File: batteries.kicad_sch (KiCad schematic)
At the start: 14 parts, among them J3 67996-110HLF

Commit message: general fixes #3 #4
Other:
- moved on the sheet: RTD1, RTD2, RTD3
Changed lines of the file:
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@@
     (effects (font (face "KiCad Font") (size 4 4)) (justify left bottom))
   )
-  (text "RTS SENSORS\n" (at 116.84 43.18 0)
+  (text "RTS SENSORS\n" (at 36.83 33.02 0)
     (effects (font (face "KiCad Font") (size 4 4)) (justify left bottom))
   )
@@
     )
   )
-  (global_label "RTD_common" (shape input) (at 132.08 76.2 180) (fields_autoplaced)
-    (effects (font (size 1.27 1.27)) (justify right))
-    (property "Intersheetrefs" "${INTERSHEET_REFS}" (at 116.6974 76.2 0)
+  (global_label "RTD_common" (shape input) (at 52.07 66.04 180) (fields_autoplaced)
+    (effects (font (size 1.27 1.27)) (justify right))
+    (property "Intersheetrefs" "${INTERSHEET_REFS}" (at 36.6874 66.04 0)
       (effects (font (size 1.27 1.27)) (justify right) hide)
     )
@@
     )
   )
-  (global_label "RTD3" (shape input) (at 142.24 76.2 0) (fields_autoplaced)
-    (effects (font (size 1.27 1.27)) (justify left))
-    (property "Intersheetrefs" "${INTERSHEET_REFS}" (at 149.9423 76.2 0)
+  (global_label "RTD3" (shape input) (at 62.23 66.04 0) (fields_autoplaced)
+    (effects (font (size 1.27 1.27)) (justify left))
+    (property "Intersheetrefs" "${INTERSHEET_REFS}" (at 69.9323 66.04 0)
       (effects (font (size 1.27 1.27)) (justify left) hide)
     )
@@
     )
   )
-  (global_label "RTD6" (shape input) (at 142.24 88.9 0) (fields_autoplaced)
-    (effects (font (size 1.27 1.27)) (justify left))
-    (property "Intersheetrefs" "${INTERSHEET_REFS}" (at 149.9423 88.9 0)
-      (effects (font (size 1.27 1.27)) (justify left) hide)
-    )
-  )
-  (global_label "RTD_common" (shape input) (at 132.08 88.9 180) (fields_autoplaced)
-    (effects (font (size 1.27 1.27)) (justify right))
-    (property "Intersheetrefs" "${INTERSHEET_REFS}" (at 116.6974 88.9 0)
+  (global_label "RTD6" (shape input) (at 62.23 78.74 0) (fields_autoplaced)
+    (effects (font (size 1.27 1.27)) (justify left))
+    (property "Intersheetrefs" "${INTERSHEET_REFS}" (at 69.9323 78.74 0)
+      (effects (font (size 1.27 1.27)) (justify left) hide)
+    )
+  )
+  (global_label "RTD_common" (shape input) (at 52.07 78.74 180) (fields_autoplaced)
+    (effects (font (size 1.27 1.27)) (justify right))
+    (property "Intersheetrefs" "${INTERSHEET_REFS}" (at 36.6874 78.74 0)
       (effects (font (size 1.27 1.27)) (justify right) hide)
     )
@@
     )
   )
-  (global_label "RTD2" (shape input) (at 142.24 63.5 0) (fields_autoplaced)
-    (effects (font (size 1.27 1.27)) (justify left))
-    (property "Intersheetrefs" "${INTERSHEET_REFS}" (at 149.9423 63.5 0)
+  (global_label "RTD2" (shape input) (at 62.23 53.34 0) (fields_autoplaced)
+    (effects (font (size 1.27 1.27)) (justify left))
+    (property "Intersheetrefs" "${INTERSHEET_REFS}" (at 69.9323 53.34 0)
       (effects (font (size 1.27 1.27)) (justify left) hide)
     )
@@
     )
   )
-  (global_label "RTD_common" (shape input) (at 132.08 63.5 180) (fields_autoplaced)
-    (effects (font (size 1.27 1.27)) (justify right))
-    (property "Intersheetrefs" "${INTERSHEET_REFS}" (at 116.6974 63.5 0)
+  (global_label "RTD_common" (shape input) (at 52.07 53.34 180) (fields_autoplaced)
+    (effects (font (size 1.27 1.27)) (justify right))
+    (property "Intersheetrefs" "${INTERSHEET_REFS}" (at 36.6874 53.34 0)
       (effects (font (size 1.27 1.27)) (justify right) hide)
     )
@@
     )
   )
-  (symbol (lib_id "Device:Thermistor") (at 137.16 88.9 90) (unit 1)
-    (in_bom yes) (on_board yes) (dnp no) (fields_autoplaced)
-    (property "Reference" "RTD1" (at 137.16 82.55 90)
-      (effects (font (size 1.27 1.27)))
-    )
-    (property "Value" "Thermistor" (at 137.16 85.09 90)
-      (effects (font (size 1.27 1.27)))
-    )
-    (property "Footprint" "" (at 137.16 88.9 0)
-      (effects (font (size 1.27 1.27)) hide)
-    )
-    (property "Datasheet" "~" (at 137.16 88.9 0)
+  (symbol (lib_id "Device:Thermistor") (at 57.15 78.74 90) (unit 1)
+    (in_bom yes) (on_board yes) (dnp no) (fields_autoplaced)
+    (property "Reference" "RTD1" (at 57.15 72.39 90)
+      (effects (font (size 1.27 1.27)))
+    )
+    (property "Value" "Thermistor" (at 57.15 74.93 90)
+      (effects (font (size 1.27 1.27)))
+    )
+    (property "Footprint" "" (at 57.15 78.74 0)
+      (effects (font (size 1.27 1.27)) hide)
+    )
+    (property "Datasheet" "~" (at 57.15 78.74 0)
       (effects (font (size 1.27 1.27)) hide)
     )
@@
     )
   )
-  (symbol (lib_id "Device:Thermistor") (at 137.16 63.5 90) (unit 1)
-    (in_bom yes) (on_board yes) (dnp no) (fields_autoplaced)
-    (property "Reference" "RTD2" (at 137.16 57.15 90)
-      (effects (font (size 1.27 1.27)))
-    )
-    (property "Value" "Thermistor" (at 137.16 59.69 90)
-      (effects (font (size 1.27 1.27)))
-    )
-    (property "Footprint" "" (at 137.16 63.5 0)
-      (effects (font (size 1.27 1.27)) hide)
-    )
-    (property "Datasheet" "~" (at 137.16 63.5 0)
+  (symbol (lib_id "Device:Thermistor") (at 57.15 53.34 90) (unit 1)
+    (in_bom yes) (on_board yes) (dnp no) (fields_autoplaced)
+    (property "Reference" "RTD2" (at 57.15 46.99 90)
+      (effects (font (size 1.27 1.27)))
+    )
+    (property "Value" "Thermistor" (at 57.15 49.53 90)
+      (effects (font (size 1.27 1.27)))
+    )
+    (property "Footprint" "" (at 57.15 53.34 0)
+      (effects (font (size 1.27 1.27)) hide)
+    )
+    (property "Datasheet" "~" (at 57.15 53.34 0)
       (effects (font (size 1.27 1.27)) hide)
     )
@@
     )
   )
-  (symbol (lib_id "Device:Thermistor") (at 137.16 76.2 90) (unit 1)
-    (in_bom yes) (on_board yes) (dnp no) (fields_autoplaced)
-    (property "Reference" "RTD3" (at 137.16 69.85 90)
-      (effects (font (size 1.27 1.27)))
-    )
-    (property "Value" "Thermistor" (at 137.16 72.39 90)
-      (effects (font (size 1.27 1.27)))
-    )
-    (property "Footprint" "" (at 137.16 76.2 0)
-      (effects (font (size 1.27 1.27)) hide)
-    )
-    (property "Datasheet" "~" (at 137.16 76.2 0)
-      (effects (font (size 1.27 1.27)) hide)
-    )
+  (symbol (lib_id "Device:Thermistor") (at 57.15 66.04 90) (unit 1)
+    (in_bom yes) (on_board yes) (dnp no) (fields_autoplaced)
+    (property "Reference" "RTD3" (at 57.15 59.69 90)
+      (effects (font (size 1.27 1.27)))
+    )
+    (property "Value" "Thermistor" (at 57.15 62.23 90)
+      (effects (font (size 1.27 1.27)))
+    )
+    (property "Footprint" "" (at 57.15 66.04 0)
+      (effects (font (size 1.27 1.27)) hide)
+    )
+    (property "Datasheet" "~" (at 57.15 66.04 0)
+      (effects (font (size 1.27 1.27)) hide)
+    )

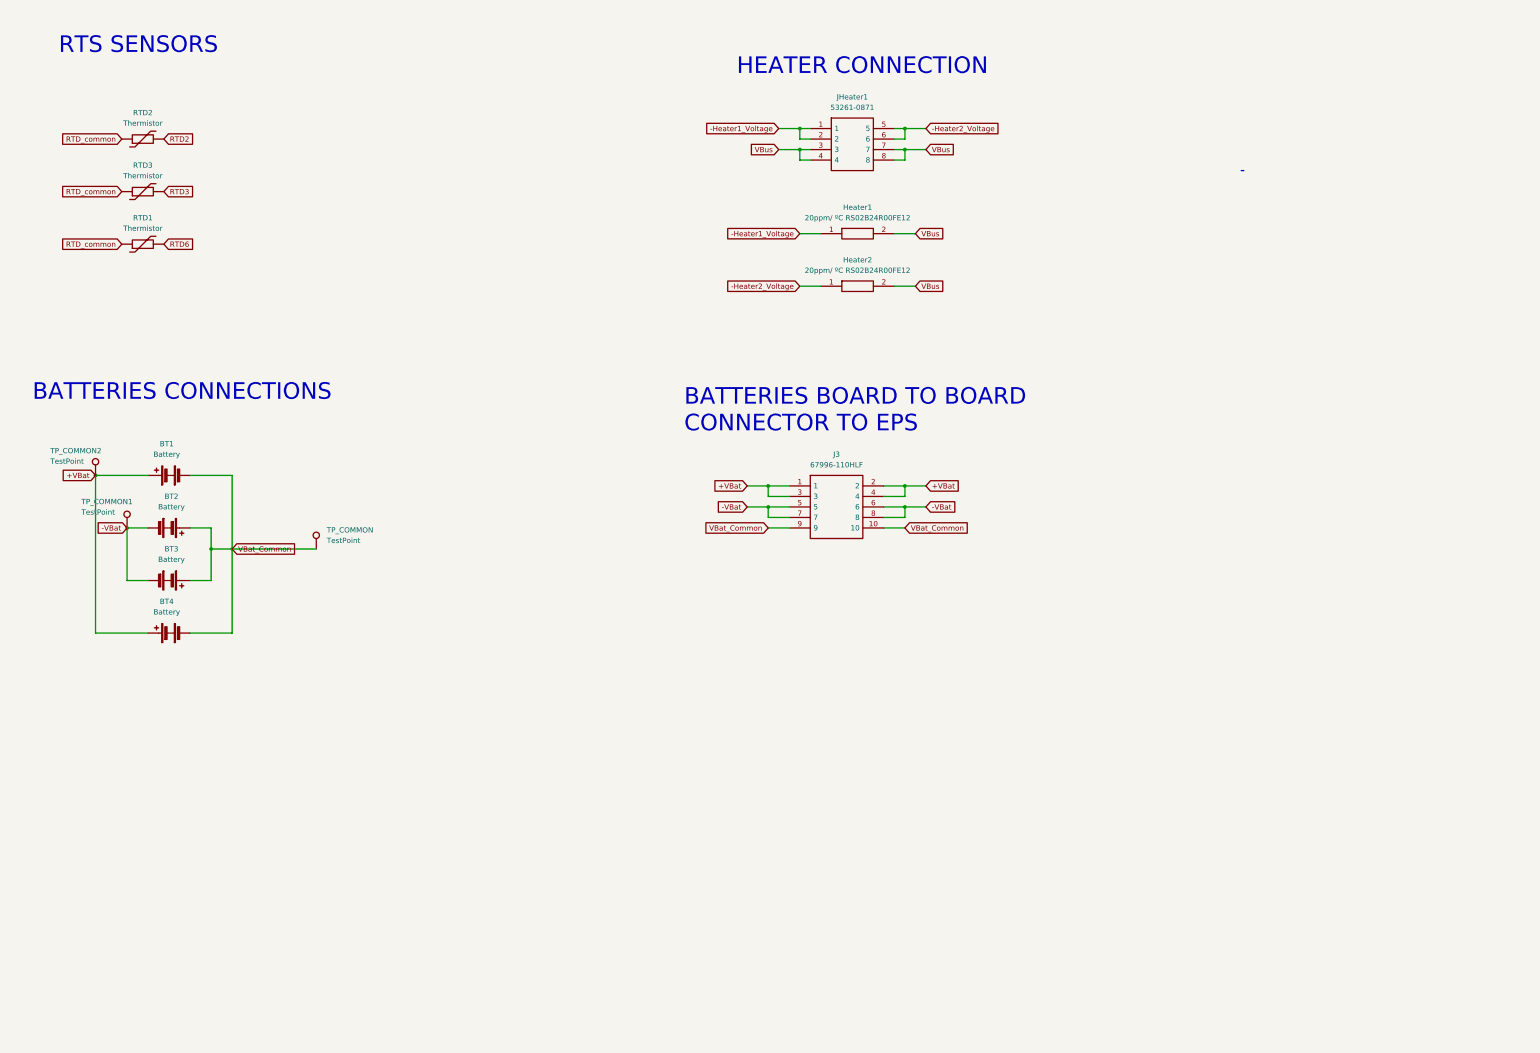
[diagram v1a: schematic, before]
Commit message: developing rtd and heater circuits
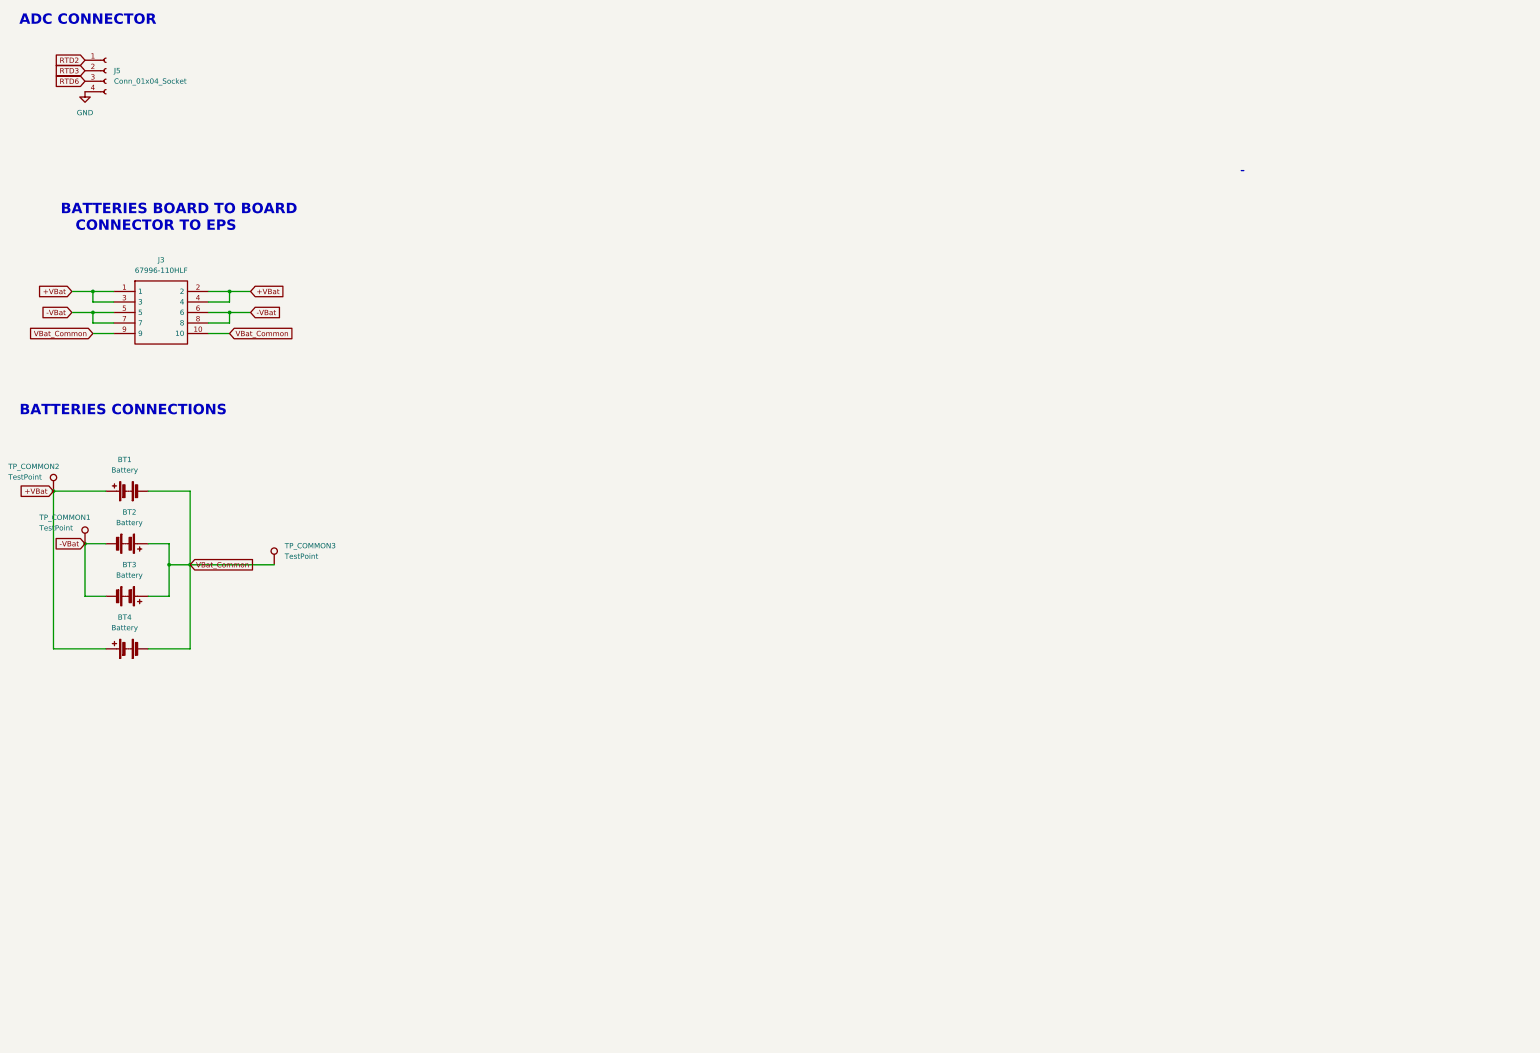
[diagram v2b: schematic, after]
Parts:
- removed Heater1, Heater2: 20ppm/ ºC RS02B24R00FE12, symbol RS02B24R00FE12:RS02B24R00FE12
- removed JHeater1: 53261-0871, symbol 53261-0871:53261-0871
- removed RTD1, RTD2, RTD3: Thermistor, symbol Device:Thermistor
- added J5: Conn_01x04_Socket, symbol Connector:Conn_01x04_Socket
- J3: footprint (none) -> lib:67996-110HLF
- renumbered TP_COMMON to TP_COMMON3
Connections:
- net RTD2: now also J5.1 (Pin_1)
- net RTD3: now also J5.2 (Pin_2)
- net RTD6: now also J5.3 (Pin_3)
- new net GND: J5.4 (Pin_4)
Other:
- note added: "ADC CONNECTOR"
- note removed: "HEATER CONNECTION"
- note removed: "RTS SENSORS"
- moved on the sheet: BT1, BT2, BT3, BT4, J3, TP_COMMON1, TP_COMMON2, TP_COMMON3

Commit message: fixing voltages and uploading heater circuit
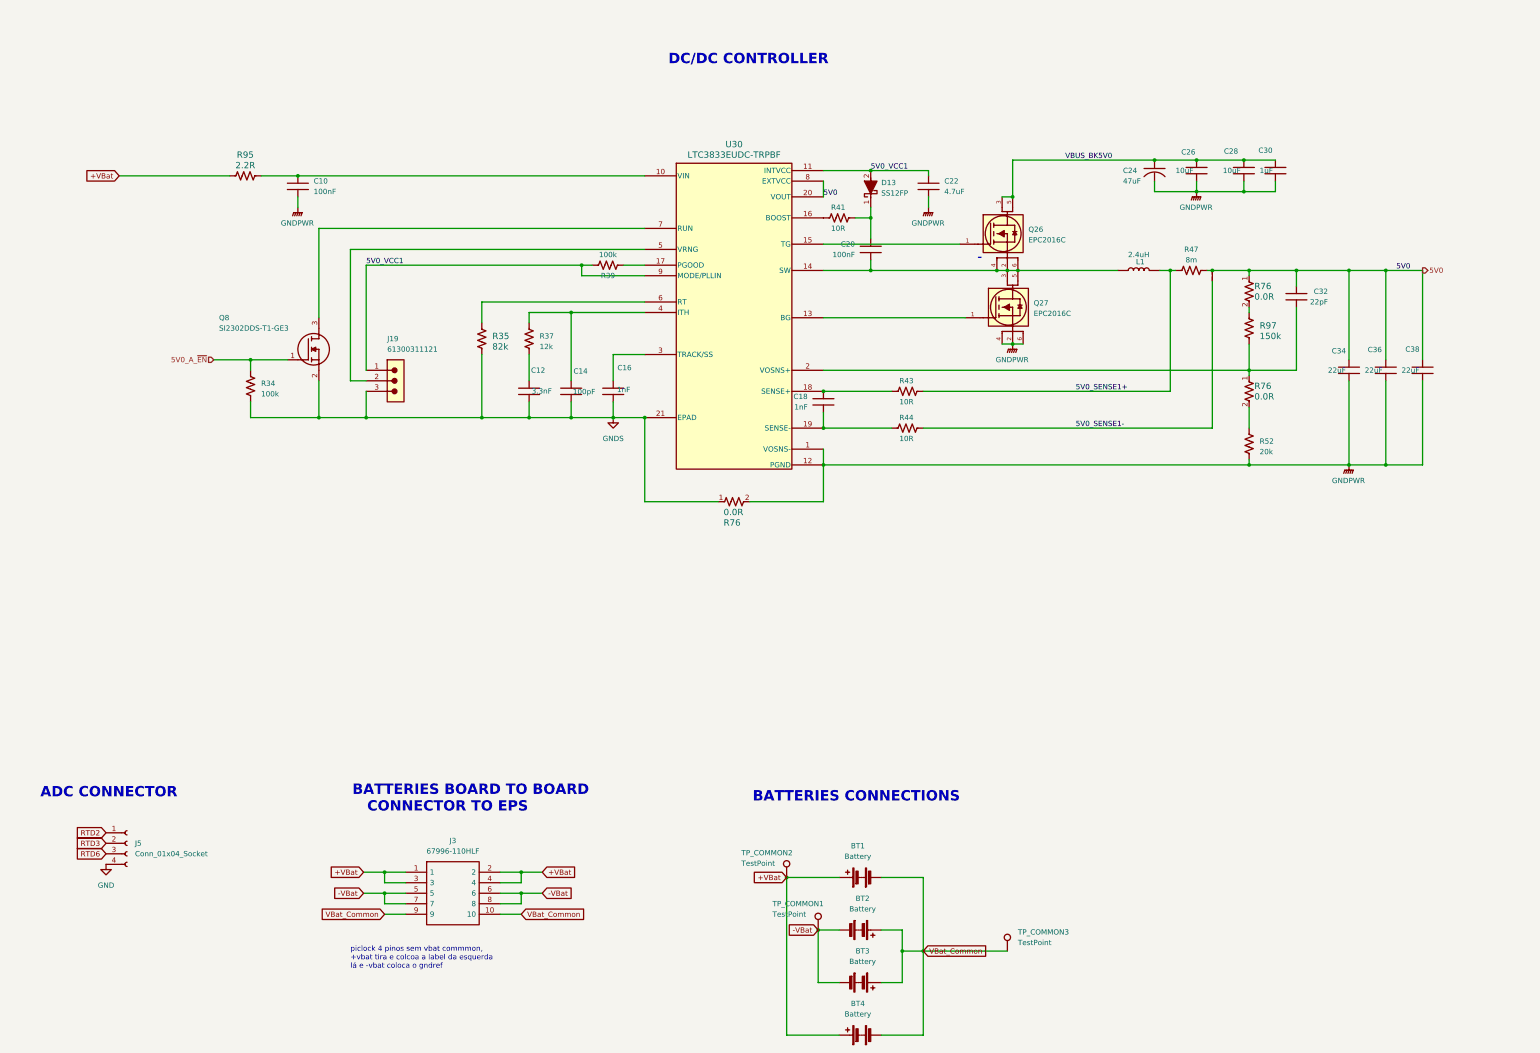
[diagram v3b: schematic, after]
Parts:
- added C10, C20: 100nF, footprints:C0603C104K5RACTU, symbol C0603C104K5RACTU:C0603C104K5RACTU
- added C12: 3.3nF, footprints:C0603C332J5GACAUTO, symbol C0603C332J5GACAUTO:C0603C332J5GACAUTO
- added C14: 100pF, footprints:C0603C101J5GACAUTO, symbol C0603C101J5GACAUTO:C0603C101J5GACAUTO
- added C16, C18: 1nF, footprints:C0603C102F3GACTU, symbol C0603C102F3GACTU:C0603C102F3GACTU
- added C22: 4.7uF, footprints:GCM32ER71H475KA55L, symbol GCM32ER71H475KA55L:GCM32ER71H475KA55L
- added C24: 47uF, footprints:T495X476K035ATE300, symbol T495X476K035ATE300:T495X476K035ATE300
- added C26, C28: 10uF, footprints:C1210C106K5RACTU, symbol C1210C106K5RACTU:C1210C106K5RACTU
- added C30: 1uF, footprints:C0805C105K5RACTU, symbol C0805C105K5RACTU:C0805C105K5RACTU
- added C32: 22pF, footprints:C0603C220K5RACAUTO, symbol C0603C220K5RACAUTO:C0603C220K5RACAUTO
- added C34, C36, C38: 22uF, footprints:GCM32ER71C226KE19L, symbol GCM32ER71C226KE19L:GCM32ER71C226KE19L
- added D13: SS12FP, footprints:SS12FP, symbol SS12FP:SS12FP
- added J19: 61300311121, footprints:three_position_jumper, symbol 61300311121:61300311121
- added JP2: SolderJumper_2_Bridged, footprints:Jumper, symbol Jumper:Jumper
- added L1: 2.4uH, footprints:744325240, symbol 744325240:744325240
- added Q26, Q27: EPC2016C, footprints:EPC2016C, symbol EPC2016C:EPC2016C
- added Q8: SI2302DDS-T1-GE3, footprints:SI2302DDS-T1-GE3, symbol SI2302DDS-T1-GE3:SI2302DDS-T1-GE3
- added R34, R39: 100k, footprints:CRCW0603100KFKEAHP, symbol CRCW0603100KFKEAHP:CRCW0603100KFKEAHP
- added R35: 82k, footprints:CRCW060382K0FKEA, symbol CRCW060382K0FKEA:CRCW060382K0FKEA
- added R37: 12k, footprints:CRCW060312K0FKEAHP, symbol CRCW060312K0FKEAHP:CRCW060312K0FKEAHP
- added R41, R43, R44: 10R, footprints:CRCW060310R0FKEAHP, symbol CRCW060310R0FKEAHP:CRCW060310R0FKEAHP
- added R47: 8m, footprints:WSL20108L000FEA18, symbol WSL20108L000FEA18:WSL20108L000FEA18
- added R52: 20k, footprints:CRCW060320K0FKEAHP, symbol CRCW060320K0FKEAHP:CRCW060320K0FKEAHP
- added R76 (x3): 0.0R, footprints:CRCW06030000Z0EAHP, symbol CRCW06030000Z0EAHP:CRCW06030000Z0EAHP
- added R95: 2.2R, footprints:CRCW06032R20FKEAHP, symbol CRCW06032R20FKEAHP:CRCW06032R20FKEAHP
- added R97: 150k, footprints:CRCW0603150KFKEAHP, symbol CRCW0603150KFKEAHP:CRCW0603150KFKEAHP
- added U30: LTC3833EUDC-TRPBF, footprints:LTC3833EUDC#TRPBF, symbol LTC3833EUDC#TRPBF:LTC3833EUDC-TRPBF
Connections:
- net +VBat: now also R95.2
- new net: C10.2, R95.1, U30.10 (VIN)
- new net: Q27.1 (Gate), U30.13 (BG)
- new net: C20.2, L1.1, Q26.2 (Substrate), Q26.4 (Source), Q26.6 (Source), Q27.3 (Drain), Q27.5 (Drain), U30.14 (SW)
- new net: Q26.1 (Gate), U30.15 (TG)
- new net: R41.2, U30.16 (BOOST)
- new net: R39.1, U30.17 (PGOOD)
- new net: C18.1, R43.2, U30.18 (SENSE+)
- new net: C18.2, R44.2, U30.19 (SENSE-)
- new net: C32.2, R76.1, R97.1, U30.2 (VOSNS+)
- new net: C16.1, U30.3 (TRACK/SS)
- new net: C14.1, R37.2, U30.4 (ITH)
- new net: J19.2, U30.5 (VRNG)
- new net: R35.2, U30.6 (RT)
- new net: Q8.3 (D), U30.7 (RUN)
- new net: R52.2, R76.2
- new net: C20.1, D13.1 (K), R41.1
- new net: R76.2, R97.2
- new net: C12.1, R37.1
- new net 5V0: C32.1, C34.2, C36.2, C38.2, JP2.2 (B), R47.1, R76.1, U30.20 (VOUT), U30.8 (EXTVCC)
- new net 5V0_A_~{EN}: Q8.1 (G), R34.2
- new net 5V0_SENSE1+: L1.2, R43.1, R47.2
- new net 5V0_SENSE1-: JP2.1 (A), R44.1
- new net 5V0_VCC1: C22.1, D13.2 (A), J19.1, R39.2, U30.11 (INTVCC), U30.9 (MODE/PLLIN)
- new net GNDPWR: C10.1, C22.2, C24.1 (CATHODE), C26.2, C28.2, C30.2, C34.1, C36.1, C38.1, Q27.2 (Substrate), Q27.4 (Source), Q27.6 (Source), R52.1, R76.2, U30.1 (VOSNS-), U30.12 (PGND)
- new net GNDS: C12.2, C14.2, C16.2, J19.3, Q8.2 (S), R34.1, R35.1, R76.1, U30.21 (EPAD)
- new net VBUS_BK5V0: C24.2 (ANODE), C26.1, C28.1, C30.1, Q26.3 (Drain), Q26.5 (Drain)
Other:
- note added: "DC/DC CONTROLLER"
- note added: "piclock 4 pinos sem vbat commmon, +vbat tira e colcoa a label da esquerda lá e -vbat coloca o gndref"
- moved on the sheet: BT1, BT2, BT3, BT4, J3, J5, TP_COMMON1, TP_COMMON2, TP_COMMON3
